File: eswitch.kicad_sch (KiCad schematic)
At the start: 153 parts, among them J1 Wuerth 691311400116, J2 +12V IN, J3 GND IN, J4 USB-C, J5 UART, SW1 RESET, SW2 BOOT, U1 BTS7008-1EPP, U10 ESP32-S3-WROOM-1-N8, U11 USBLC6-2SC6, U2 BTS7008-1EPP, U3 BTS7008-1EPP, U4 BTS7008-1EPP, U5 BTS7008-1EPP, U6 BTS7008-1EPP, U7 BTS7008-1EPP, U8 BTS7008-1EPP, U9 TPS54360B

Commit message: BOM: manufacturer + MPN for every part, DigiKey upload CSV, off-board extras
Co-Authored-By: Claude Fable 5.1 <noreply@anthropic.com>
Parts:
- C1, C2: MPN (none) -> GRM32ER71H475KA88L; Manufacturer (none) -> Murata
- C10, C3, C4: MPN (none) -> CL10B104KB8NNNC; Manufacturer (none) -> Samsung Electro-Mechanics
- C101, C201, C301, C401, C501, C601, C701, C801: MPN (none) -> CL21B104KBCNNNC; Manufacturer (none) -> Samsung Electro-Mechanics
- C102, C202, C302, C402, C502, C602, C702, C802: MPN (none) -> CL21B103KBANNNC; Manufacturer (none) -> Samsung Electro-Mechanics
- C103, C203, C303, C403, C503, C603, C703, C803: MPN (none) -> CL10C221JB8NNNC; Manufacturer (none) -> Samsung Electro-Mechanics
- C11: MPN (none) -> CL10B105KO8NNNC; Manufacturer (none) -> Samsung Electro-Mechanics
- C5: MPN (none) -> CL10B273KB8NNNC; Manufacturer (none) -> Samsung Electro-Mechanics
- C6: MPN (none) -> CL10C151JB8NNNC; Manufacturer (none) -> Samsung Electro-Mechanics
- C7, C8: MPN (none) -> GRM32ER71A226KE20L; Manufacturer (none) -> Murata
- C9: MPN (none) -> CL21A106KPFNNNE; Manufacturer (none) -> Samsung Electro-Mechanics
- D1, D2, D4: MPN (none) -> B360-13-F; Manufacturer (none) -> Diodes Incorporated
- D101, D201, D301, D401, D501, D601, D701, D801: MPN (none) -> BAT54S,215; Manufacturer (none) -> Nexperia
- D102, D202, D302, D402, D502, D602, D702, D802: MPN (none) -> 150060GS75000; Manufacturer (none) -> Wurth Elektronik
- D3: MPN (none) -> SMBJ26A; Manufacturer (none) -> Littelfuse
- D5: MPN (none) -> 150060BS75000; Manufacturer (none) -> Wurth Elektronik
- F1, F2, F3, F4, F5, F6, F7, F8: MPN Keystone 3557 (x3) -> 3557; Manufacturer (none) -> Keystone Electronics; Note AUTO: fuse in COM-SW; BYPASS: fuse in COM-LOAD -> 3 clips per position; AUTO: fuse in COM-SW; BYPASS: fuse in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
- F9: MPN Littelfuse 0466002.NR -> 0466002.NR; Manufacturer (none) -> Littelfuse
- J1: Manufacturer (none) -> Wurth Elektronik
- J2, J3: MPN Keystone 8196 -> 8196; Manufacturer (none) -> Keystone Electronics
- J4: MPN GCT USB4105-GF-A -> USB4105-GF-A; Manufacturer (none) -> GCT
- J5: MPN (none) -> 61300411121; Manufacturer (none) -> Wurth Elektronik
- L1: MPN Bourns SRP7028A-100M -> SRP7028A-100M; Manufacturer (none) -> Bourns
- R1: MPN (none) -> RC0603FR-07200KL; Manufacturer (none) -> YAGEO
- R101, R102, R105, R201, R202, R205, R301, R302, R305, R401, R402, R405, R501, R502, R505, R601, R602, R605, R701, R702, R705, R801, R802, R805: MPN (none) -> RC0603FR-074K7L; Manufacturer (none) -> YAGEO
- R103, R203, R303, R403, R503, R603, R703, R803: MPN (none) -> RC0805FR-0747RL; Manufacturer (none) -> YAGEO
- R104, R204, R304, R404, R504, R604, R704, R804: MPN (none) -> RC0603FR-071K2L; Manufacturer (none) -> YAGEO
- R106, R206, R306, R406, R506, R606, R706, R806: MPN (none) -> RC0603FR-0747KL; Manufacturer (none) -> YAGEO
- R107, R207, R307, R407, R507, R607, R707, R807: MPN (none) -> RC0603FR-072K2L; Manufacturer (none) -> YAGEO
- R2: MPN (none) -> RC0603FR-0731K6L; Manufacturer (none) -> YAGEO
- R3: MPN (none) -> RC0603FR-0710K2L; Manufacturer (none) -> YAGEO
- R4: MPN (none) -> RC0603FR-073K9L; Manufacturer (none) -> YAGEO
- R5, R6: MPN (none) -> RC0603FR-0710KL; Manufacturer (none) -> YAGEO
- R7, R8: MPN (none) -> RC0603FR-075K1L; Manufacturer (none) -> YAGEO
- R9: MPN (none) -> RC0603FR-071KL; Manufacturer (none) -> YAGEO
- SW1, SW2: Manufacturer (none) -> C&K
- U1, U2, U3, U4, U5, U6, U7, U8: Manufacturer (none) -> Infineon
- U10: Manufacturer (none) -> Espressif
- U11: Manufacturer (none) -> STMicroelectronics
- U9: Manufacturer (none) -> Texas Instruments

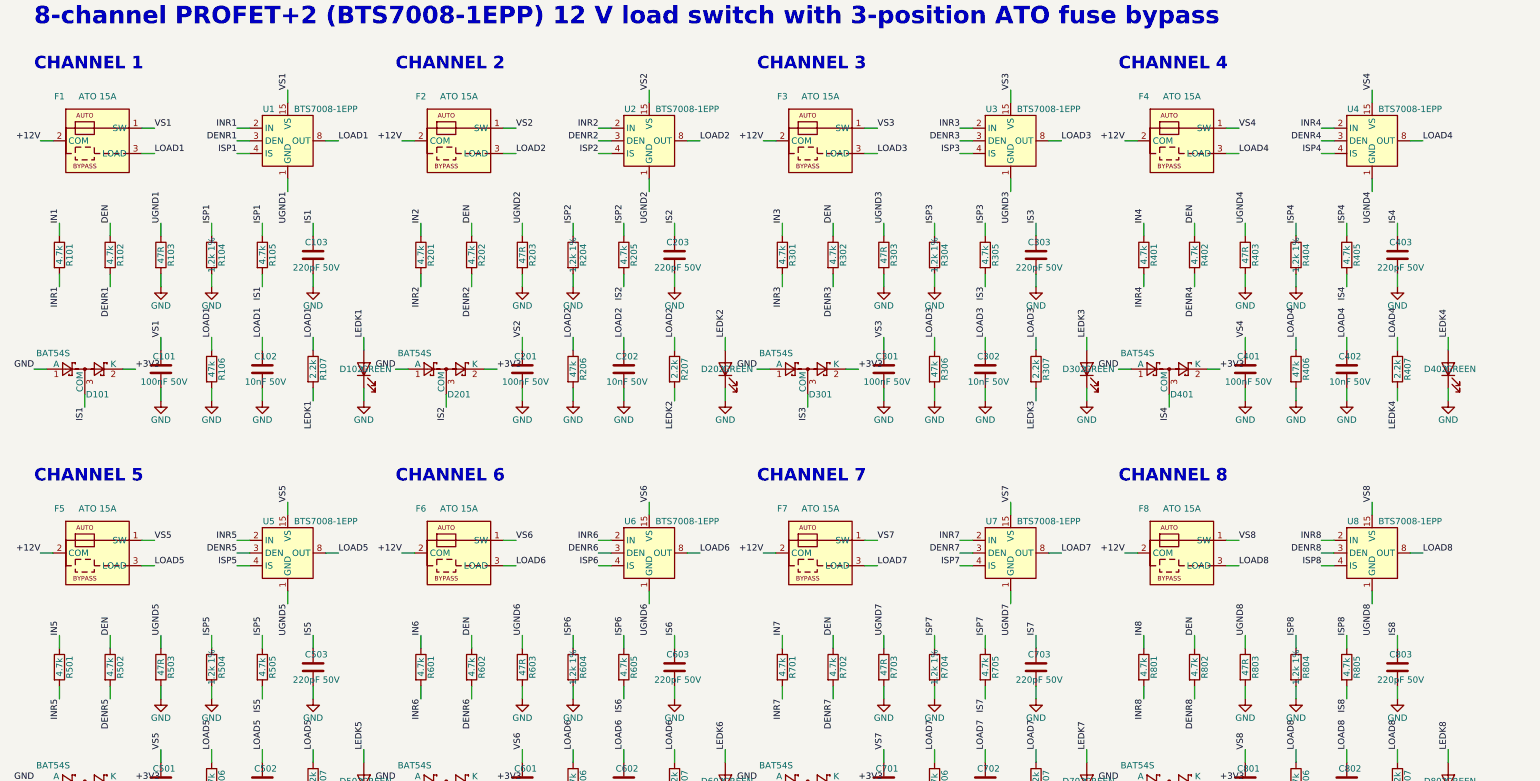
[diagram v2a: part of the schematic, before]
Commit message: Channel ratings 2x10A/5x5A/1x20A with BTS7004/7008/7002, 1 oz copper strategy, USB-C tie-off rework
Co-Authored-By: Claude Fable 5.1 <noreply@anthropic.com>
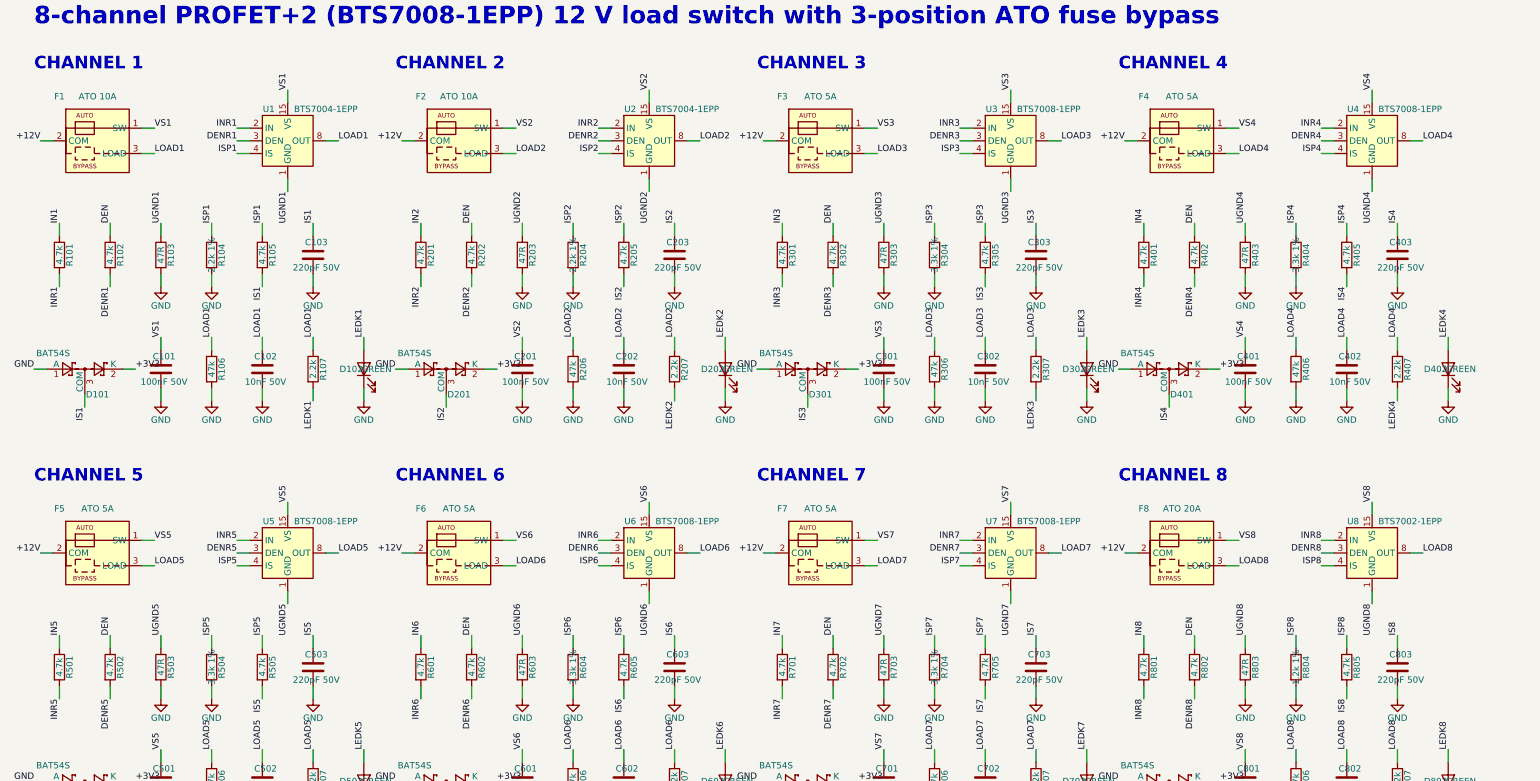
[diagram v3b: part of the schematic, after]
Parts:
- F1: value ATO 15A -> ATO 10A; Note 3 clips per position; AUTO: fuse in COM-SW; BYPASS: fuse in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 -> 3 clips per position; CH1 10 A; AUTO: fuse in COM-SW; BYPAS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
- F2: value ATO 15A -> ATO 10A; Note 3 clips per position; AUTO: fuse in COM-SW; BYPASS: fuse in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 -> 3 clips per position; CH2 10 A; AUTO: fuse in COM-SW; BYPAS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
- F3: value ATO 15A -> ATO 5A; Note 3 clips per position; AUTO: fuse in COM-SW; BYPASS: fuse in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 -> 3 clips per position; CH3 5 A; AUTO: fuse in COM-SW; BYPASS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
- F4: value ATO 15A -> ATO 5A; Note 3 clips per position; AUTO: fuse in COM-SW; BYPASS: fuse in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 -> 3 clips per position; CH4 5 A; AUTO: fuse in COM-SW; BYPASS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
- F5: value ATO 15A -> ATO 5A; Note 3 clips per position; AUTO: fuse in COM-SW; BYPASS: fuse in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 -> 3 clips per position; CH5 5 A; AUTO: fuse in COM-SW; BYPASS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
- F6: value ATO 15A -> ATO 5A; Note 3 clips per position; AUTO: fuse in COM-SW; BYPASS: fuse in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 -> 3 clips per position; CH6 5 A; AUTO: fuse in COM-SW; BYPASS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
- F7: value ATO 15A -> ATO 5A; Note 3 clips per position; AUTO: fuse in COM-SW; BYPASS: fuse in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 -> 3 clips per position; CH7 5 A; AUTO: fuse in COM-SW; BYPASS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
- F8: value ATO 15A -> ATO 20A; Note 3 clips per position; AUTO: fuse in COM-SW; BYPASS: fuse in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 -> 3 clips per position; CH8 20 A; AUTO: fuse in COM-SW; BYPAS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
- R104, R204: value 1.2k 1% -> 2.2k 1%; MPN RC0603FR-071K2L -> RC0603FR-072K2L
- R304, R404, R504, R604, R704: value 1.2k 1% -> 3.3k 1%; MPN RC0603FR-071K2L -> RC0603FR-073K3L
- U1: value BTS7008-1EPP -> BTS7004-1EPP; symbol eswitch:BTS7008-1EPP -> eswitch:BTS7004-1EPP; MPN BTS70081EPRXUMA1 -> BTS70041EPPXUMA1; Note (none) -> CH1 10 A
- U2: value BTS7008-1EPP -> BTS7004-1EPP; symbol eswitch:BTS7008-1EPP -> eswitch:BTS7004-1EPP; MPN BTS70081EPRXUMA1 -> BTS70041EPPXUMA1; Note (none) -> CH2 10 A
- U3: Note (none) -> CH3 5 A
- U4: Note (none) -> CH4 5 A
- U5: Note (none) -> CH5 5 A
- U6: Note (none) -> CH6 5 A
- U7: Note (none) -> CH7 5 A
- U8: value BTS7008-1EPP -> BTS7002-1EPP; symbol eswitch:BTS7008-1EPP -> eswitch:BTS7002-1EPP; MPN BTS70081EPRXUMA1 -> BTS70021EPPXUMA1; Note (none) -> CH8 20 A

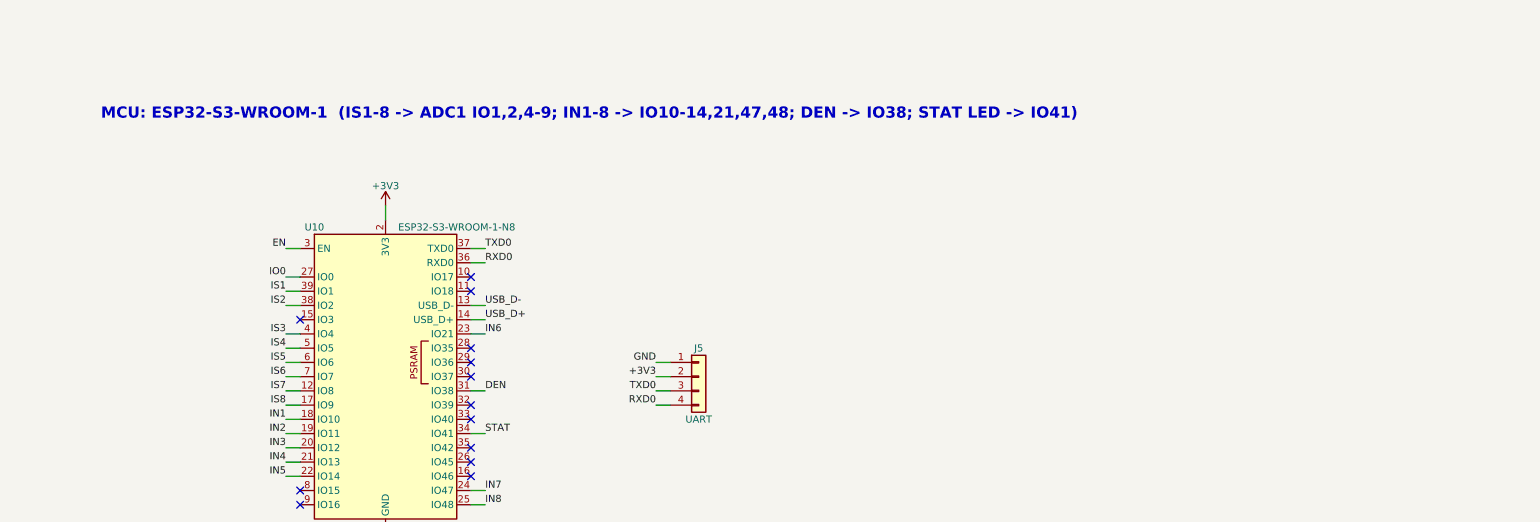
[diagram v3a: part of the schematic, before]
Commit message: Routed 1 oz board: 2x10A/5x5A/1x20A channels, DRC clean (0 copper violations, 0 unconnected)
- BTS7004/7008/7002 per rating, per-channel RSENSE, CH8 (20 A) with parallel In2 copper
- IS4 moved to IO2; decoupling/pull-ups re-placed; USB-C D+/D- tie-offs on opposite sides
- finish.py: post-route prune, fix-ups, clearance-checked grid router for hand routes
- fab/: regenerated gerbers, BOMs (DigiKey/JLCPCB/PCBWay), CPLs, 1 oz stack-up note

Co-Authored-By: Claude Fable 5.1 <noreply@anthropic.com>
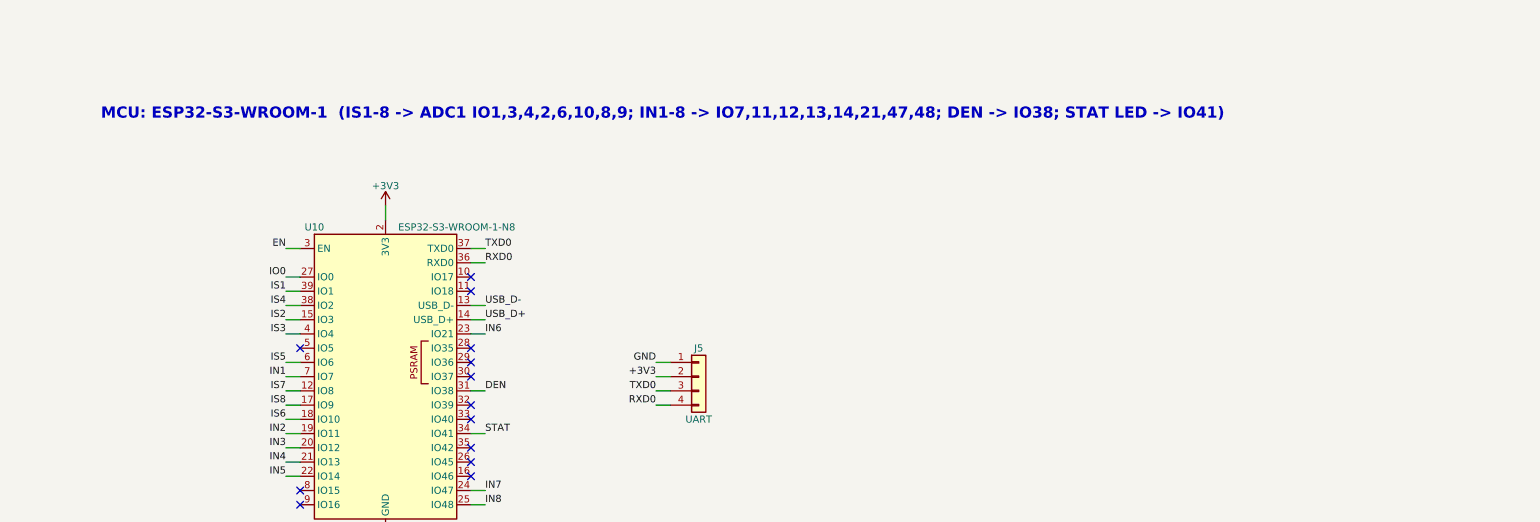
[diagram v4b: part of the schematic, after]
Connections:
- net IN1: now also U10.7 (IO7); no longer U10.18 (IO10)
- net IS2: now also U10.15 (IO3); no longer U10.38 (IO2)
- net IS4: now also U10.38 (IO2); no longer U10.5 (IO5)
- net IS6: now also U10.18 (IO10); no longer U10.7 (IO7)
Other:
- note added: "MCU: ESP32-S3-WROOM-1 (IS1-8 -> ADC1 IO1,3,4,2,6,10,8,9; IN1-8 -> IO7,11,12,13,14,21,47,48; DEN -> IO38; STAT LED -> IO41)"
- note removed: "MCU: ESP32-S3-WROOM-1 (IS1-8 -> ADC1 IO1,2,4-9; IN1-8 -> IO10-14,21,47,48; DEN -> IO38; STAT LED -> IO41)"
